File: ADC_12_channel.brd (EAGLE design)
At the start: 148.1 x 127 mm, 165 parts, among them IC1 LM317BD2T, IC2 LM317BD2T, K1 691131710003, K2 691101710002, K3 691101710002, K4 691101710002, K5 691101710002, K6 691101710002, K7 691101710002, K8 691101710002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

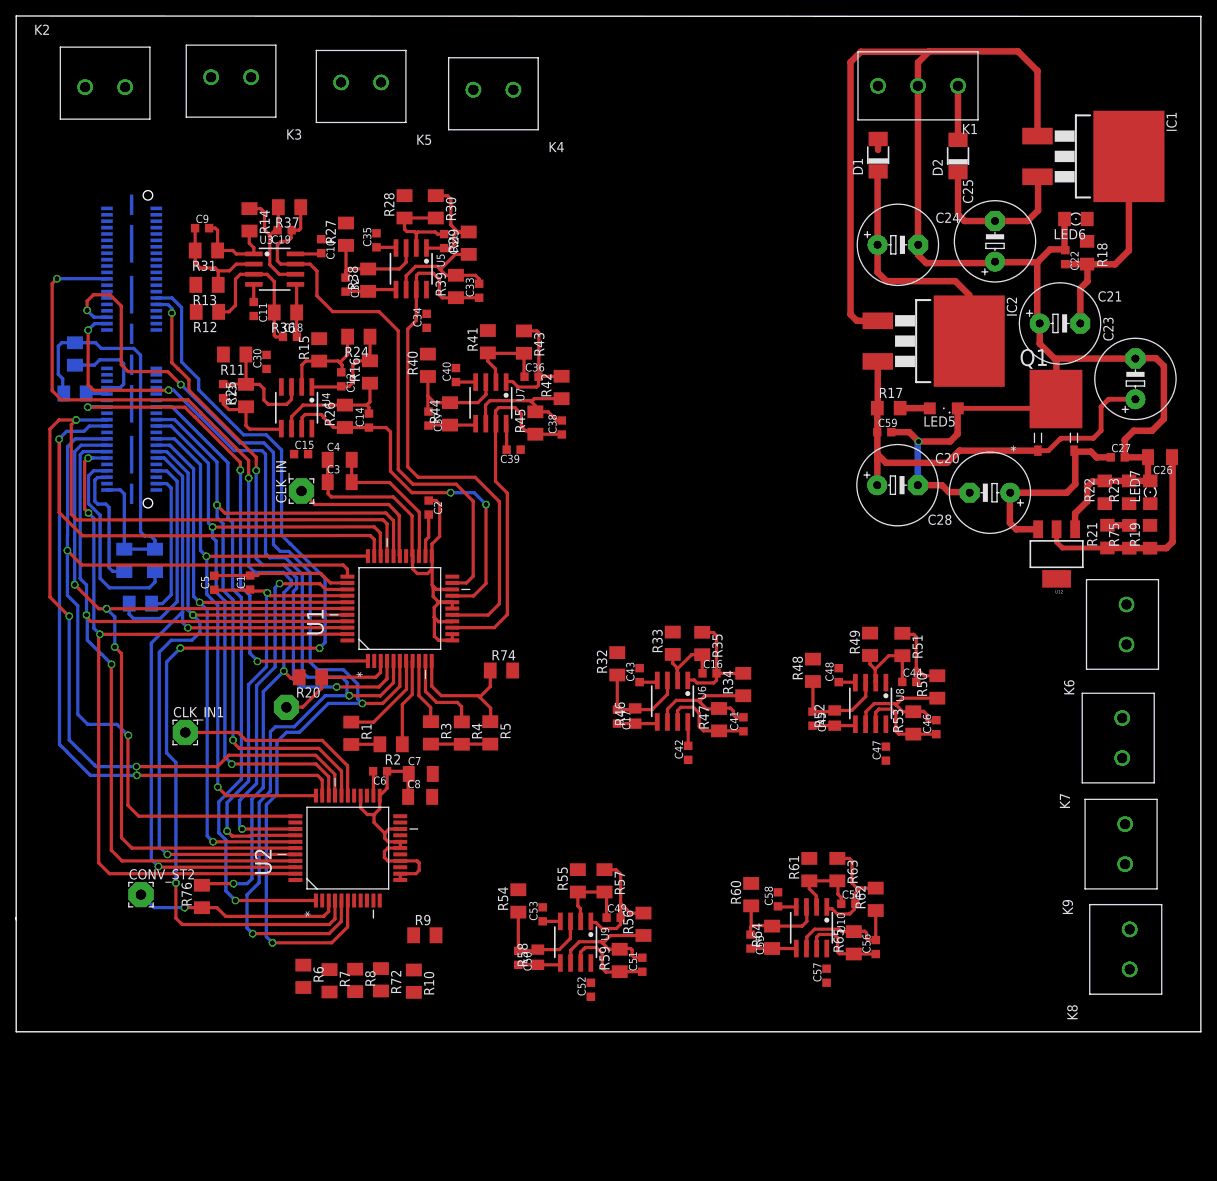
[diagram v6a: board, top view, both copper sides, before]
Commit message: Arranged & Connected ADC2 opamps
Arranged & connected ADC2 opampms
Arranged & connected i/p header for ADC1 opamps
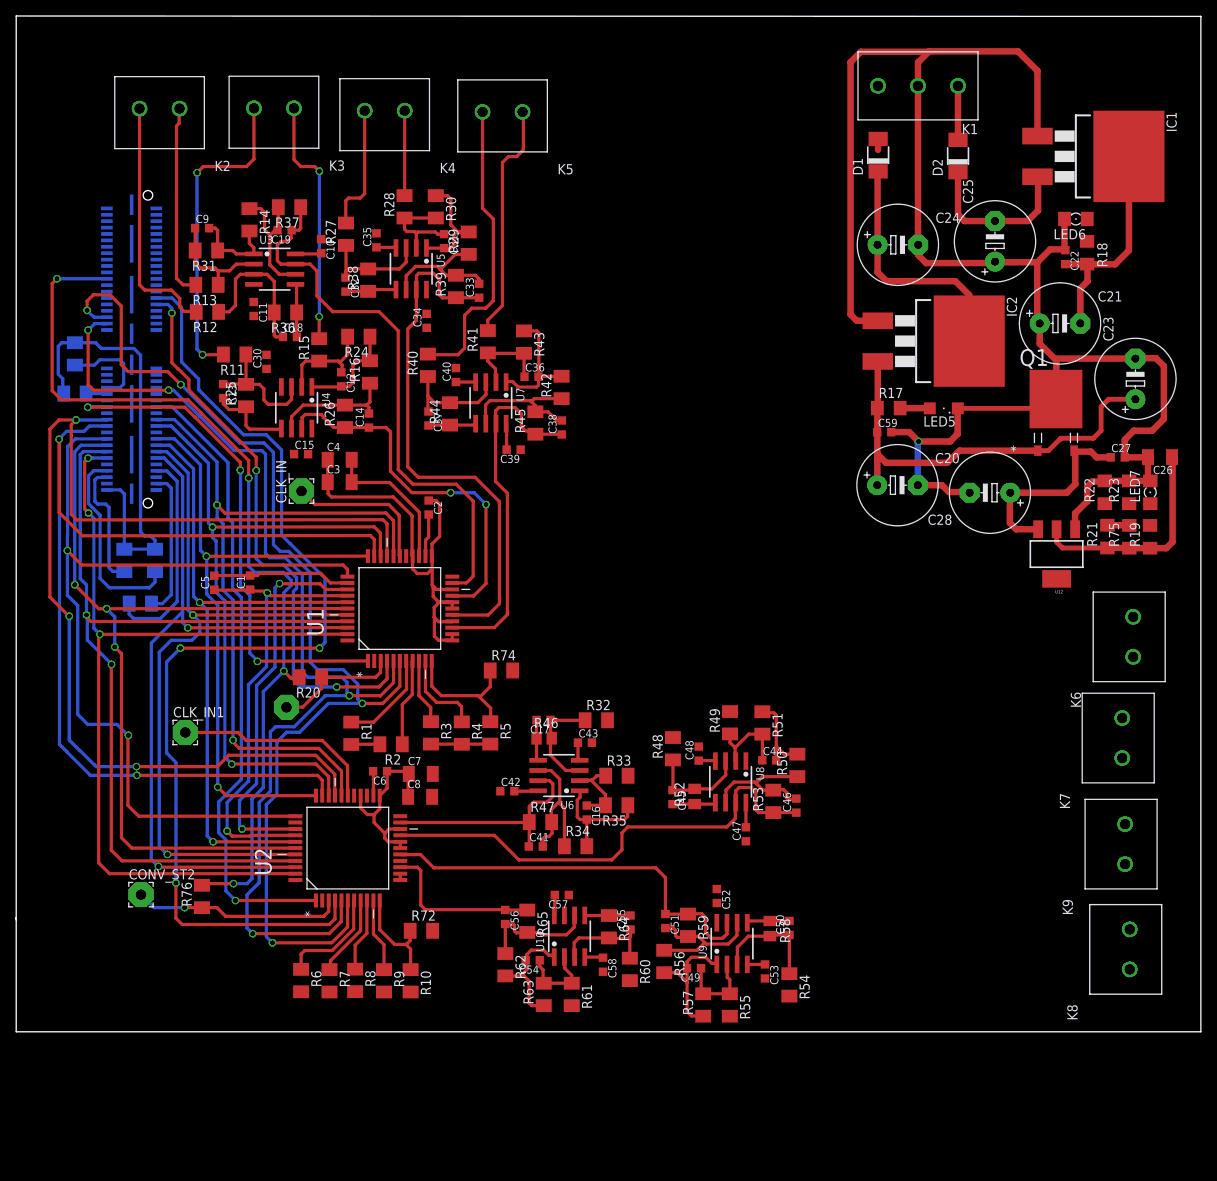
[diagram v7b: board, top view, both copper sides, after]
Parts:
- moved R62 47.0 mm to (56.9, -26.1), turned to 270 degrees
- moved C56 46.5 mm to (56.9, -20.2), turned to 270 degrees
- moved R65 40.9 mm to (59.6, -20.7), turned to 270 degrees
- moved C54 40.1 mm to (60.3, -25.6), turned to 180 degrees
- moved R63 39.9 mm to (61.7, -29.8), turned to 90 degrees
- moved R54 35.5 mm to (92.4, -28.7), turned to 270 degrees
- moved C57 34.6 mm to (63.9, -17.4), turned to 180 degrees
- moved C50 34.1 mm to (92.4, -21.5), turned to 90 degrees
- moved R61 33.5 mm to (65.2, -29.8), turned to 270 degrees
- moved U10 30.3 mm to (64.9, -22.6), turned to 0 degrees
- moved C41 30.1 mm to (60.7, -11.4), turned to 0 degrees
- moved R58 29.2 mm to (89.9, -21.6), turned to 270 degrees
- moved R34 29.1 mm to (65.7, -11.3), turned to 0 degrees
- moved C53 28.7 mm to (89.3, -27.0), turned to 270 degrees
- moved R47 25.7 mm to (61.3, -8.31), turned to 0 degrees
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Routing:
- net ADC6: track 11.8 -> 60.3 mm
- net N$28: track 0.00 -> 39.8 mm, vias 0 -> 2
- net ADC7: track 11.7 -> 50.6 mm
- net N$66: track 0.00 -> 37.6 mm
- net N$54: track 0.00 -> 31.1 mm
- net N$31: track 0.00 -> 31.1 mm, vias 0 -> 2
- net N$67: track 0.00 -> 29.8 mm
- net N$32: track 0.00 -> 24.1 mm
- net ADC5: track 12.1 -> 28.2 mm
- net N$53: track 0.00 -> 15.9 mm
- net N$23: track 0.00 -> 13.4 mm
- net N$26: track 0.00 -> 13.0 mm
- net AGND: track 145.1 -> 134.1 mm
- net N$57: track 0.00 -> 10.6 mm
- net N$22: track 0.00 -> 10.2 mm
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
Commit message: arranged & connected ADC2 headers
Routed +12_VCC
Routed VDD
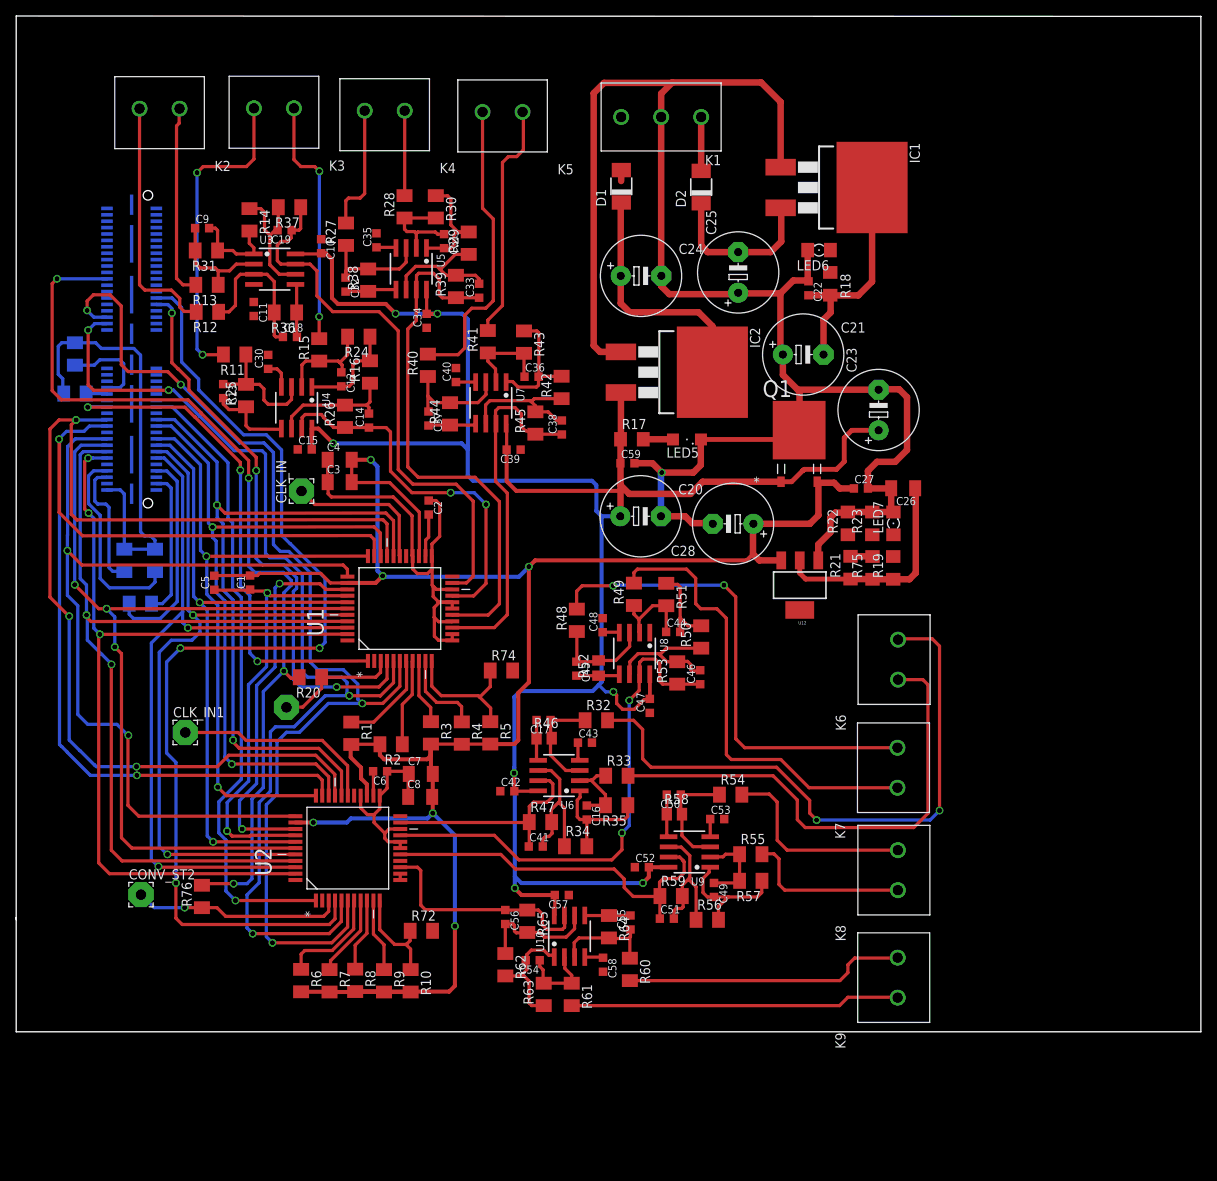
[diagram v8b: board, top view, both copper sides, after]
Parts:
- moved K9 33.0 mm to (105.9, -25.2)
- moved C22 32.3 mm to (94.8, 58.4)
- moved C28 32.3 mm to (85.3, 29.0)
- moved C59 32.3 mm to (72.1, 36.6)
- moved D1 32.3 mm to (71.4, 71.2)
- moved LED5 32.3 mm to (79.6, 39.5)
- moved LED6 32.3 mm to (96.1, 63.2)
- moved R22 32.3 mm to (99.7, 29.0)
- moved R23 32.3 mm to (102.7, 29.0)
- moved C20 32.3 mm to (73.8, 29.9)
- moved C21 32.3 mm to (94.1, 50.1)
- moved C23 32.3 mm to (103.5, 43.2)
- moved C24 32.3 mm to (73.8, 60.0)
- moved C25 32.3 mm to (86.0, 60.4)
- moved C27 32.3 mm to (101.3, 33.4)
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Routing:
- net VCC_12+: track 68.4 -> 279.7 mm, vias 0 -> 7
- net VDD: track 72.0 -> 260.3 mm, vias 0 -> 6
- net N$43: track 0.00 -> 76.3 mm, vias 0 -> 2
- net N$44: track 0.00 -> 62.4 mm
- net N$72: track 0.00 -> 61.5 mm, vias 0 -> 2
- net N$73: track 0.00 -> 57.6 mm
- net N$85: track 0.00 -> 41.2 mm
- net N$84: track 0.00 -> 35.2 mm
- net N$78: track 0.00 -> 25.2 mm
- net N$79: track 0.00 -> 20.8 mm
- net ADC8: track 20.6 -> 28.7 mm
- net ADC6: track 60.3 -> 64.2 mm, vias 0 -> 2
- net ADC7: track 50.6 -> 47.0 mm
- net VCC_12-: track 42.1 -> 45.7 mm
